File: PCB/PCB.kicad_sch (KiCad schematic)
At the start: 0 parts

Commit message: USB-C + protection
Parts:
- added J1: USB_C_Receptacle_USB2.0_16P, symbol Connector:USB_C_Receptacle_USB2.0_16P
- added R1, R2: 5.1K, symbol Device:R
- added U2: USBLC6-2SC6, Package_TO_SOT_SMD:SOT-23-6, symbol Power_Protection:USBLC6-2SC6
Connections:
- new net: J1.A5 (CC1), R1.1
- new net: J1.B5 (CC2), R2.1
- new net +5V: J1.A4 (VBUS), J1.A9 (VBUS), J1.B4 (VBUS), J1.B9 (VBUS), U2.5 (VBUS)
- new net D+: U2.4 (I/O2)
- new net D-: U2.6 (I/O1)
- new net GND: J1.A1 (GND), J1.A12 (GND), J1.B1 (GND), J1.B12 (GND), J1.S1 (SHIELD), R1.2, R2.2, U2.2 (GND)
- new net USB_D+: J1.A6 (D+), J1.B6 (D+), U2.3 (I/O2)
- new net USB_D-: J1.A7 (D-), J1.B7 (D-), U2.1 (I/O1)
- no-connect marks 0 -> 2

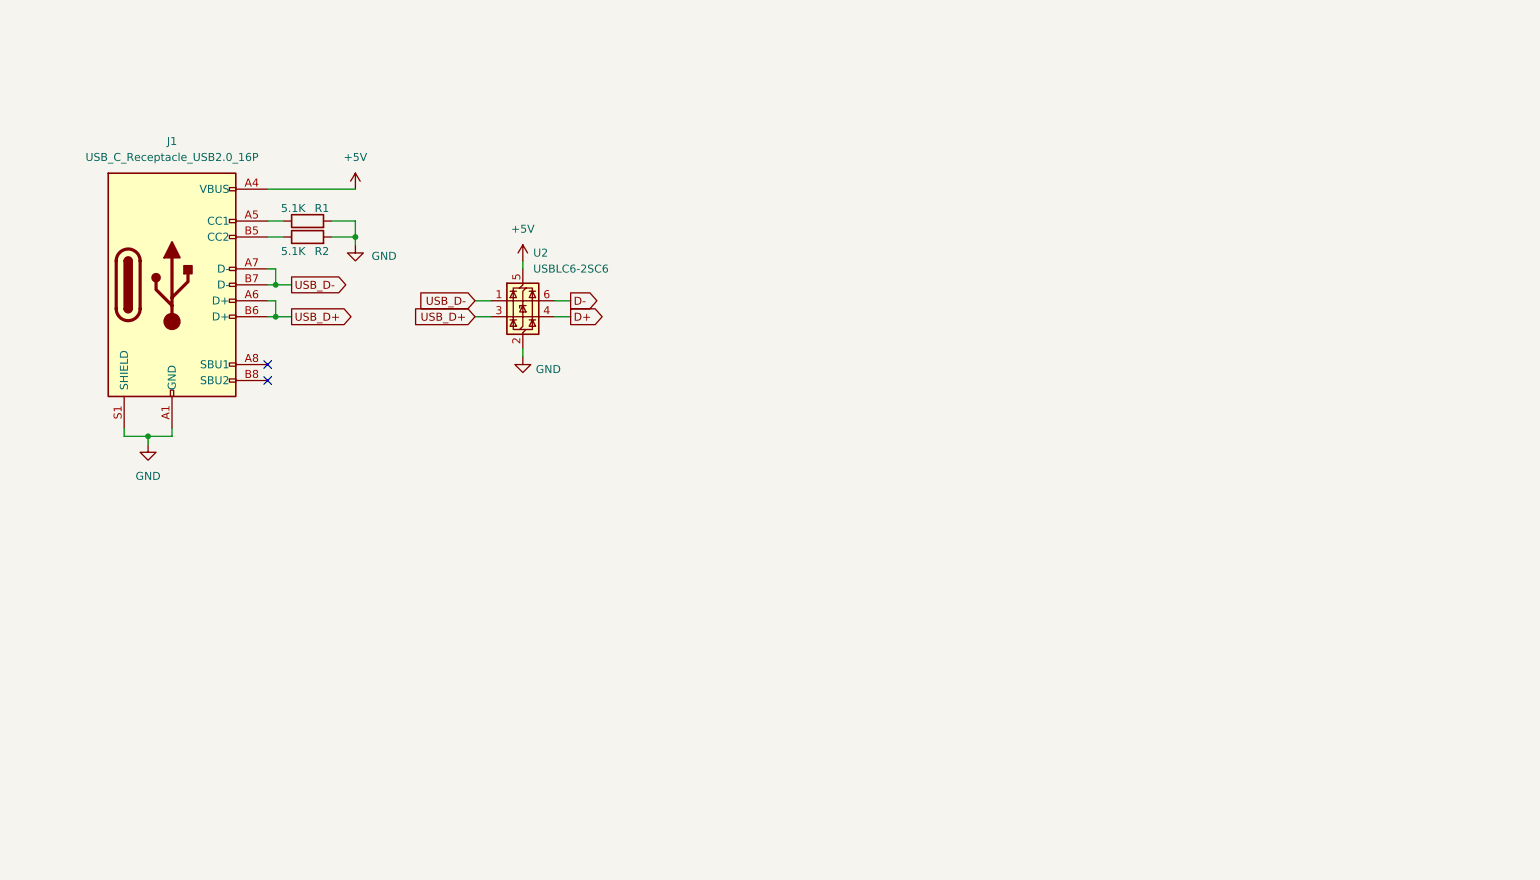
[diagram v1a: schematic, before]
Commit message: finishing power, adding in the rp2040
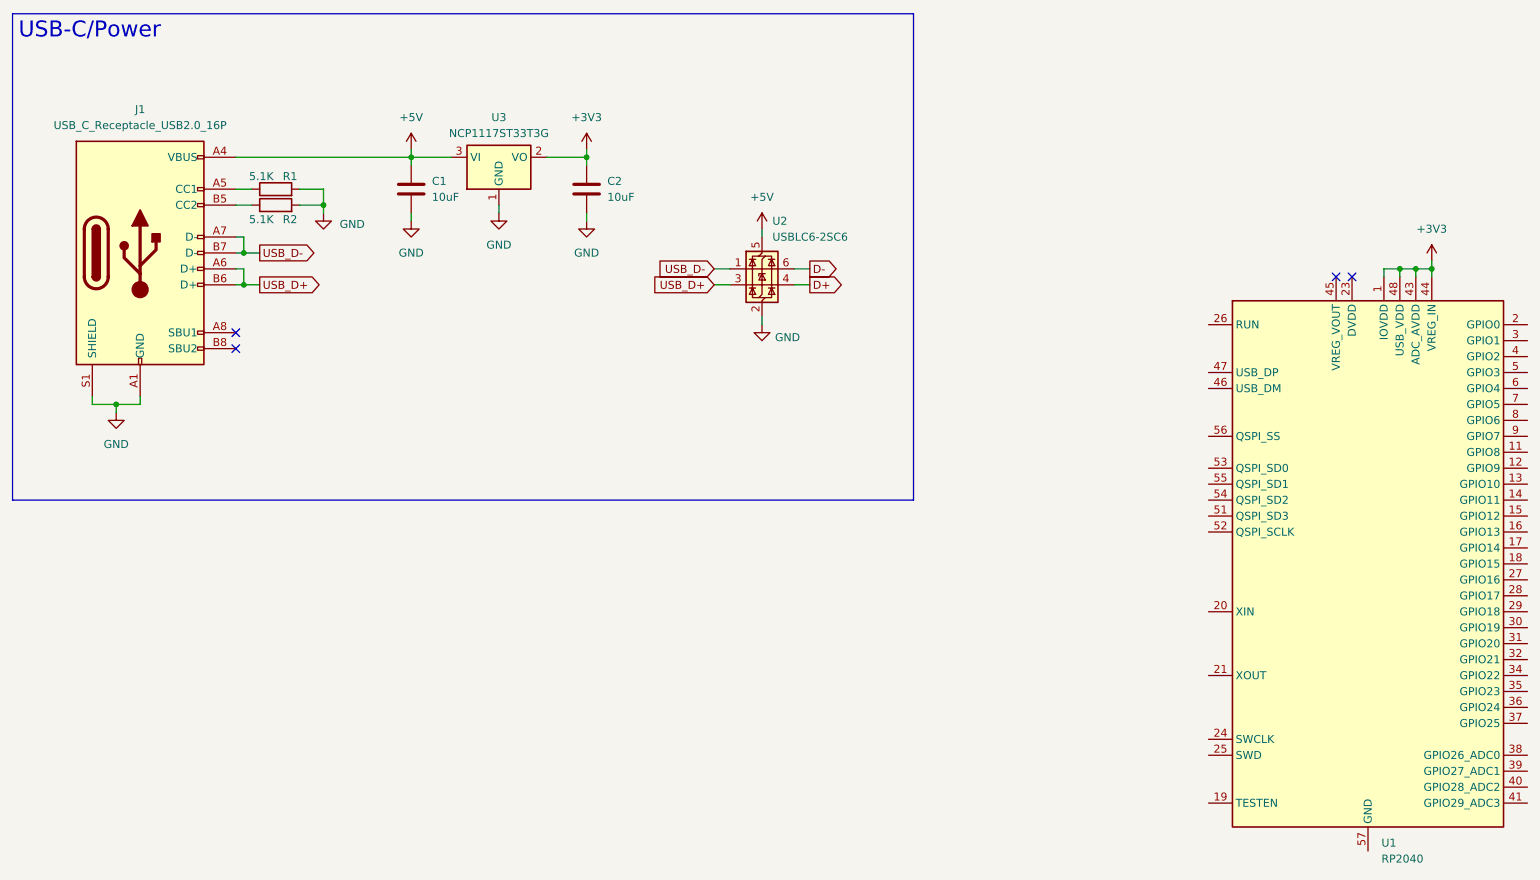
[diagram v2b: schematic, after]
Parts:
- added C1, C2: 10uF, symbol Device:C
- added U1: RP2040, Package_DFN_QFN:QFN-56-1EP_7x7mm_P0.4mm_EP3.2x3.2mm, symbol MCU_RaspberryPi:RP2040
- added U3: NCP1117ST33T3G, Package_TO_SOT_SMD:SOT-223-3_TabPin2, symbol Regulator_Linear:NCP1117-3.3_SOT223
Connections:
- net +5V: now also C1.1, U3.3 (VI)
- net GND: now also C1.2, C2.2, U3.1 (GND)
- new net: U1.23 (DVDD), U1.50 (DVDD)
- new net +3V3: C2.1, U1.1 (IOVDD), U1.10 (IOVDD), U1.22 (IOVDD), U1.33 (IOVDD), U1.42 (IOVDD), U1.43 (ADC_AVDD), U1.44 (VREG_IN), U1.48 (USB_VDD), U1.49 (IOVDD), U3.2 (VO)
- no-connect marks 2 -> 4
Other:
- moved on the sheet: J1, R1, R2, U2

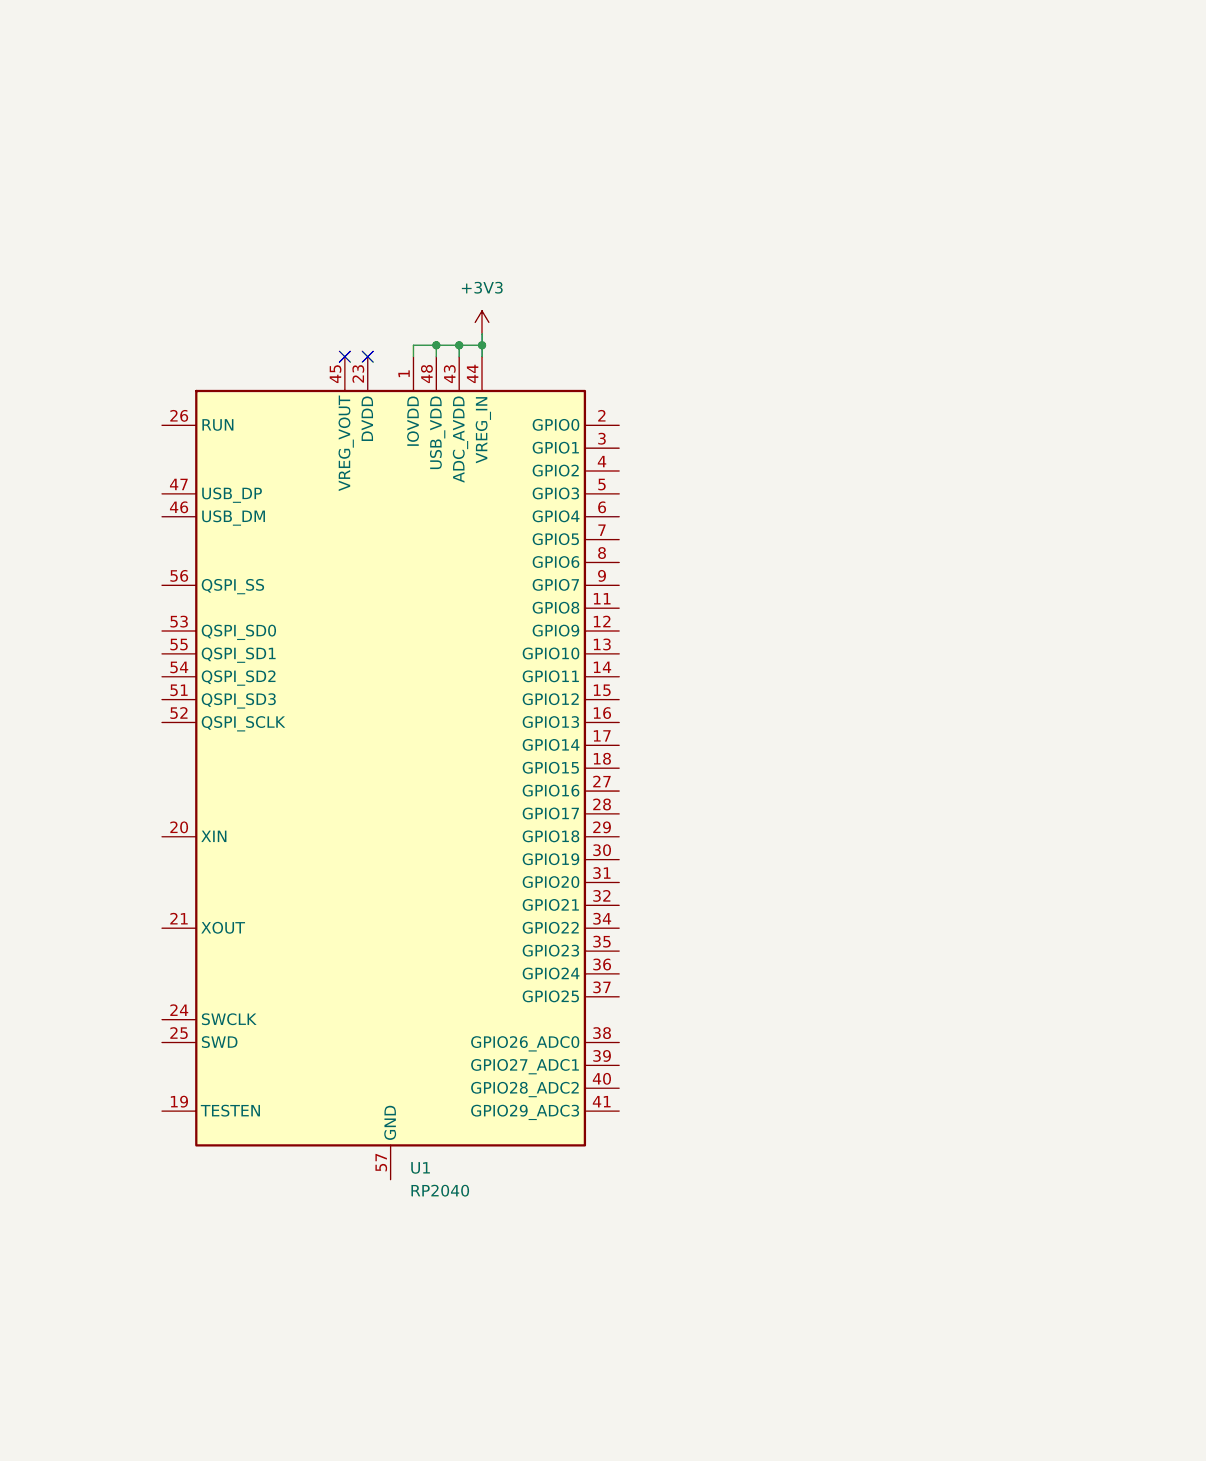
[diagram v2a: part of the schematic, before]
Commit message: adding the decoupling and grounding
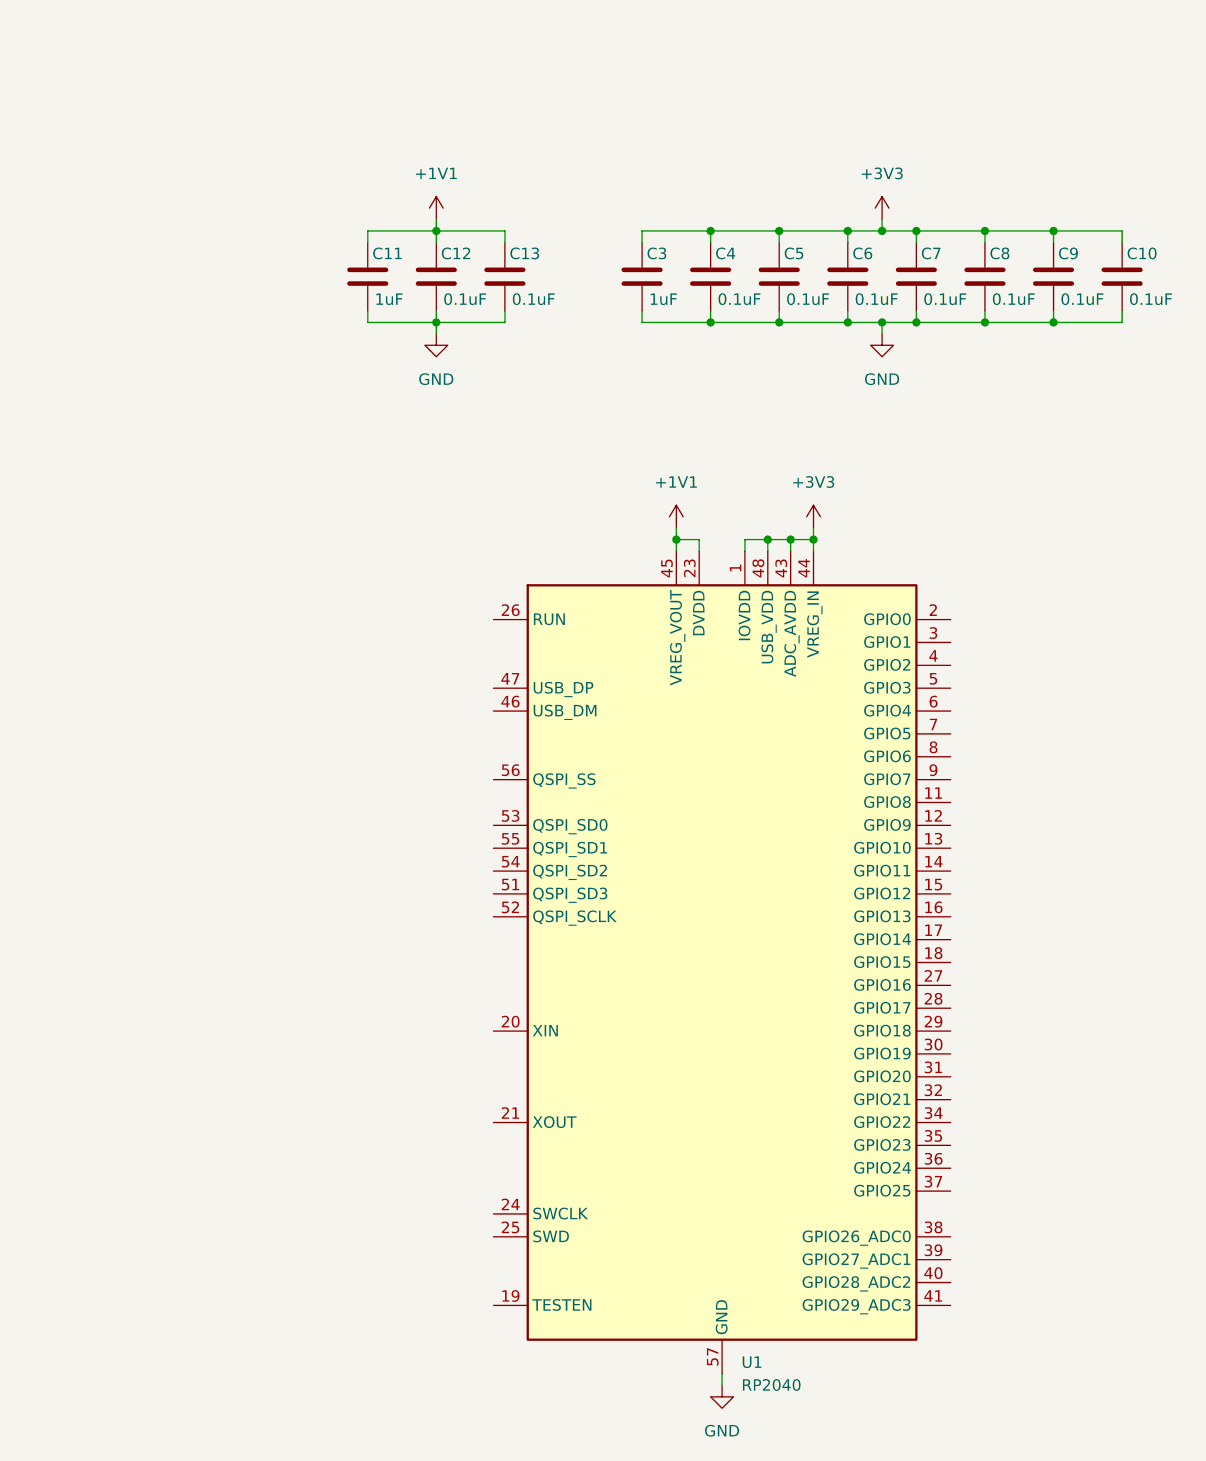
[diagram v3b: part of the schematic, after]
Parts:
- added C10, C12, C13, C4, C5, C6, C7, C8, C9: 0.1uF, symbol Device:C
- added C11, C3: 1uF, symbol Device:C
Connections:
- net +3V3: now also C10.1, C3.1, C4.1, C5.1, C6.1, C7.1, C8.1, C9.1
- net GND: now also U1.57 (GND), C10.2, C11.2, C12.2, C13.2, C3.2, C4.2, C5.2, C6.2, C7.2, C8.2, C9.2
- net +1V1: now reaches U1.23 (DVDD), U1.50 (DVDD)
- net +1V1: now also U1.45 (VREG_VOUT), C11.1, C12.1, C13.1
- no-connect marks 4 -> 2
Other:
- moved on the sheet: U1

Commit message: crystal and reset
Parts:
- added C14, C15: 33pF, symbol Device:C
- added R3, R4: 22, symbol Device:R
- added R5: 10K, symbol Device:R
- added R6: 1K, symbol Device:R
- added SW1: SW_Push, symbol Switch:SW_Push
- added Y1: Crystal_GND24, symbol Device:Crystal_GND24
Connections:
- net +3V3: now also R5.1
- net GND: now also C14.1, C15.1, SW1.1, Y1.2, Y1.4
- net USB_D+: now also R3.1
- net USB_D-: now also R4.1
- net XIN: now reaches U1.20 (XIN)
- net XIN: now also C14.2, Y1.3
- net XOUT: now reaches U1.21 (XOUT)
- net XOUT: now also R6.2
- net RESET: now reaches U1.26 (RUN)
- net RESET: now also R5.2, SW1.2
- net at U1.46 (USB_DM): now also R4.2
- net at U1.47 (USB_DP): now also R3.2
- new net: C15.2, R6.1, Y1.1
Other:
- moved on the sheet: C10, C11, C12, C13, C3, C4, C5, C6, C7, C8, C9, U1
